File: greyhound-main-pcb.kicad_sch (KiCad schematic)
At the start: 105 parts, among them J1 Conn_01x03, J12 Conn_01x03, J13 613012243121, J16 2x20_P2.54mm_Pinheader, J17 Conn_01x03, J18 2x20_P2.54mm_Pinheader, J19 Conn_01x02, J2 Conn_01x03, J20 USB_C, J3 613012243121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

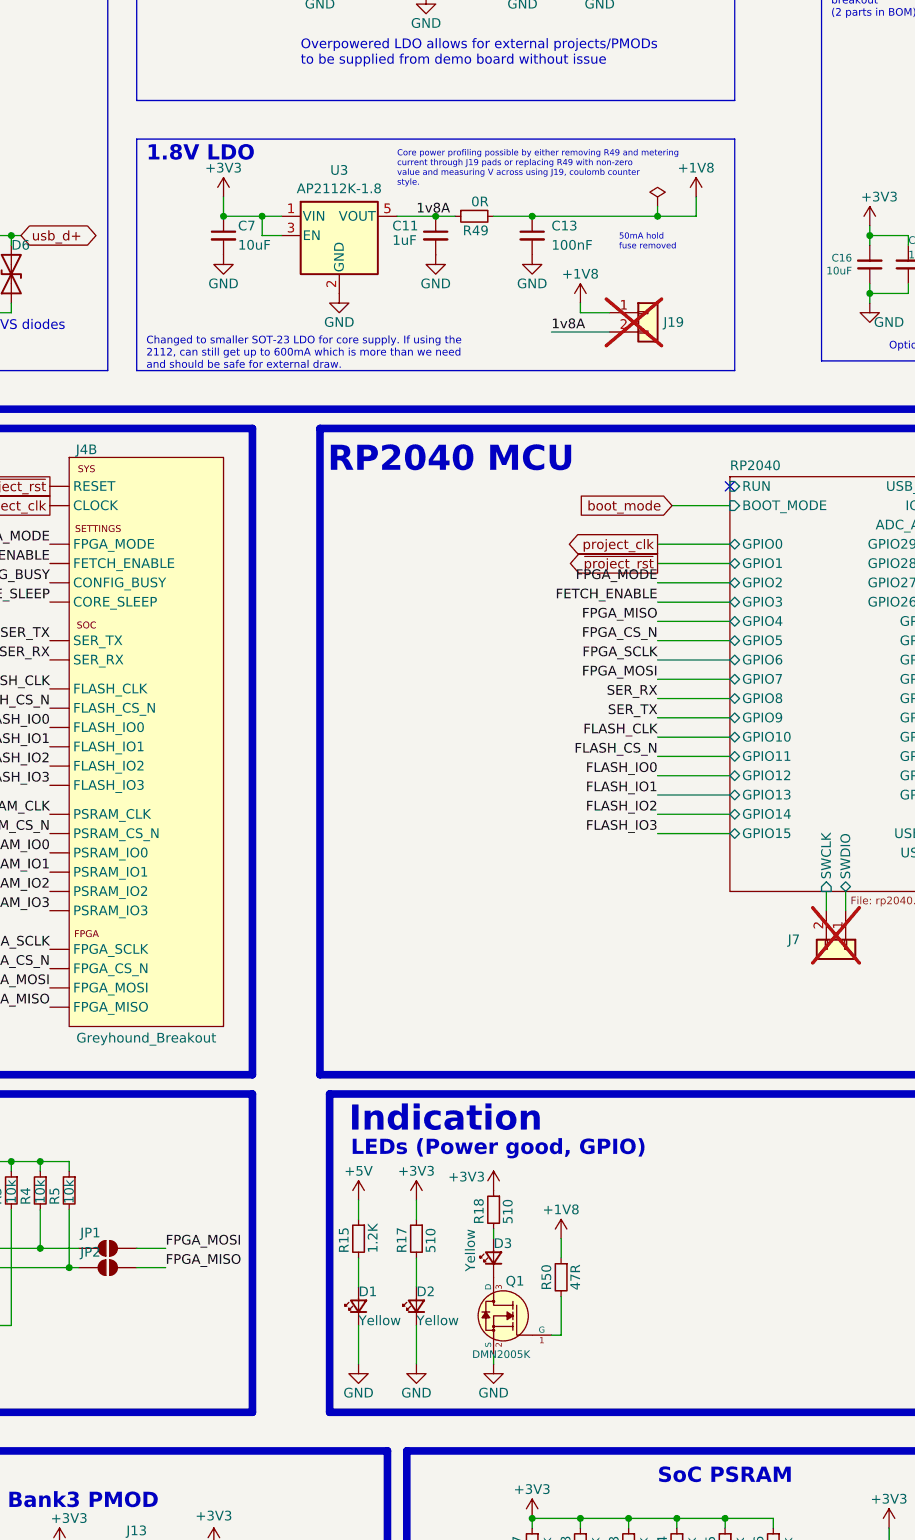
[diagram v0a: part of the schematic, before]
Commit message: Remove 1V8 LDO
Signed-off-by: Leo Moser <leomoser99@gmail.com>
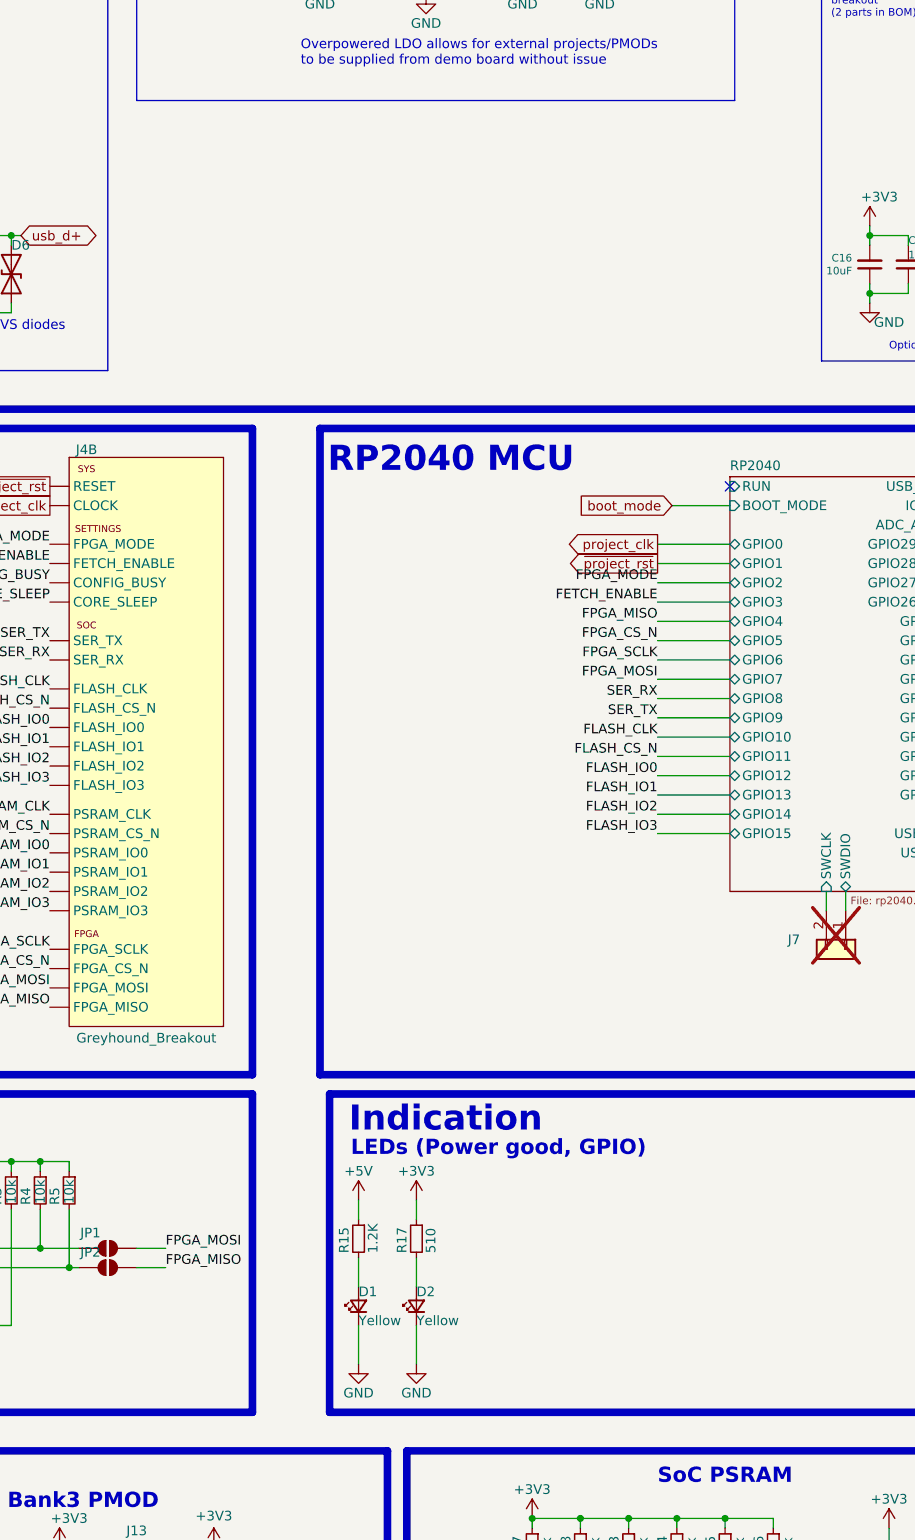
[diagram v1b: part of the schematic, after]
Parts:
- removed C11: 1uF, Capacitor_SMD:C_0603_1608Metric, symbol Device:C_Small
- removed C13: 100nF, Capacitor_SMD:C_0402_1005Metric, symbol Device:C_Small
- removed C7: 10uF, Capacitor_SMD:C_0805_2012Metric, symbol Device:C_Small
- removed D3: Yellow, LED_SMD:LED_0603_1608Metric, symbol Device:LED_Small
- removed J19: Conn_01x02, Connector_PinHeader_2.54mm:PinHeader_1x02_P2.54mm_Vertical, symbol Connector_Generic:Conn_01x02
- removed Q1: DMN2005K, Package_TO_SOT_SMD:SOT-23, symbol psychogenic:DMN2005K
- removed R18: 510, Resistor_SMD:R_0402_1005Metric, symbol Device:R_Small
- removed R49: 0R, Resistor_SMD:R_0603_1608Metric, symbol Device:R_Small
- removed R50: 47R, Resistor_SMD:R_0402_1005Metric, symbol Device:R_Small
- removed U3: AP2112K-1.8, Package_TO_SOT_SMD:SOT-23-5, symbol Regulator_Linear:AP2112K-1.8
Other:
- note removed: "1.8V LDO"
- note removed: "50mA hold fuse removed"
- note removed: "Changed to smaller SOT-23 LDO for core supply. If using the 2112, can still get up to 600mA which is more than we need and should be safe for external draw."
- note removed: "Core power profiling possible by either removing R49 and metering current through J19 pads or replacing R49 with non-zero value and measuring V across using J19, coulomb counter style."

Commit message: Update README, add images
Signed-off-by: Leo Moser <leomoser99@gmail.com>
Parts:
- FB1: LCSC C2649119 -> C14709; MPN MFBM1V1608-121-R -> BLM18PG121SN1D
- J13, J3, J5, J6: LCSC C6147817 -> C22373932
- J4: now left out of the parts list
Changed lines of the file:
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@@
 			)
 		)
-		(property "LCSC" "C6147817"
+		(property "LCSC" "C22373932"
 			(at 179.07 251.46 0)
 			(effects
@@
 			)
 		)
-		(property "LCSC" "C6147817"
+		(property "LCSC" "C22373932"
 			(at 132.08 251.46 0)
 			(effects
@@
 		(unit 2)
 		(exclude_from_sim no)
-		(in_bom yes)
+		(in_bom no)
 		(on_board yes)
 		(dnp no)
@@
 			)
 		)
-		(property "LCSC" "C6147817"
+		(property "LCSC" "C22373932"
 			(at 40.64 251.46 0)
 			(effects
@@
 			)
 		)
-		(property "LCSC" "C6147817"
+		(property "LCSC" "C22373932"
 			(at 86.36 251.46 0)
 			(effects
@@
 		(unit 1)
 		(exclude_from_sim no)
-		(in_bom yes)
+		(in_bom no)
 		(on_board yes)
 		(dnp no)
@@
 			)
 		)
-		(property "MPN" "MFBM1V1608-121-R"
+		(property "MPN" "BLM18PG121SN1D"
 			(at 161.29 31.75 90)
 			(effects
@@
 			)
 		)
-		(property "LCSC" "C2649119"
+		(property "LCSC" "C14709"
 			(at 161.29 31.75 0)
 			(effects
@@
 		(unit 3)
 		(exclude_from_sim no)
-		(in_bom yes)
+		(in_bom no)
 		(on_board yes)
 		(dnp no)
